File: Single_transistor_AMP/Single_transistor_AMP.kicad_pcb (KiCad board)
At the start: 2 copper layers, 1 part, among them Q1 BC337

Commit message: Pabeigts 7.lekcijas treniņuzdevums (P.Settings, L.Setup, D.Rules)
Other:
- net class Power added: clearance 0.5, trace_width 0.3, via_dia 1, via_drill 0.6
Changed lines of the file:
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@@
-(kicad_pcb (version 20171130) (host pcbnew "(5.1.0)-1")
+(kicad_pcb (version 20171130) (host pcbnew "(5.0.1)-4")
   (general
     (thickness 1.6)
@@
   )
   (page A4)
+  (title_block
+    (title Single_transistor_AMP)
+    (date 2019-05-03)
+    (rev v1.0)
+    (company "Ventspils Augstskola")
+    (comment 1 Autors)
+    (comment 2 "Edgars Irbiņš")
+    (comment 3 "PCB_CAD kurss")
+  )
   (layers
     (0 F.Cu signal)
@@
     (zone_45_only no)
     (trace_min 0.2)
+    (segment_width 0.2)
+    (edge_width 0.05)
     (via_size 0.8)
     (via_drill 0.4)
@@
     (uvia_min_size 0.2)
     (uvia_min_drill 0.1)
-    (edge_width 0.05)
-    (segment_width 0.2)
     (pcb_text_width 0.3)
     (pcb_text_size 1.5 1.5)
@@
     (solder_mask_min_width 0.25)
     (aux_axis_origin 0 0)
-    (visible_elements FFFFFF7F)
+    (visible_elements 7FFFFFFF)
     (pcbplotparams
       (layerselection 0x010fc_ffffffff)
@@
     (add_net "Net-(J2-Pad2)")
   )
+  (net_class Power ""
+    (clearance 0.5)
+    (trace_width 0.3)
+    (via_dia 1)
+    (via_drill 0.6)
+    (uvia_dia 0.3)
+    (uvia_drill 0.1)
+  )
   (module Package_TO_SOT_THT:TO-92_Inline (layer F.Cu)

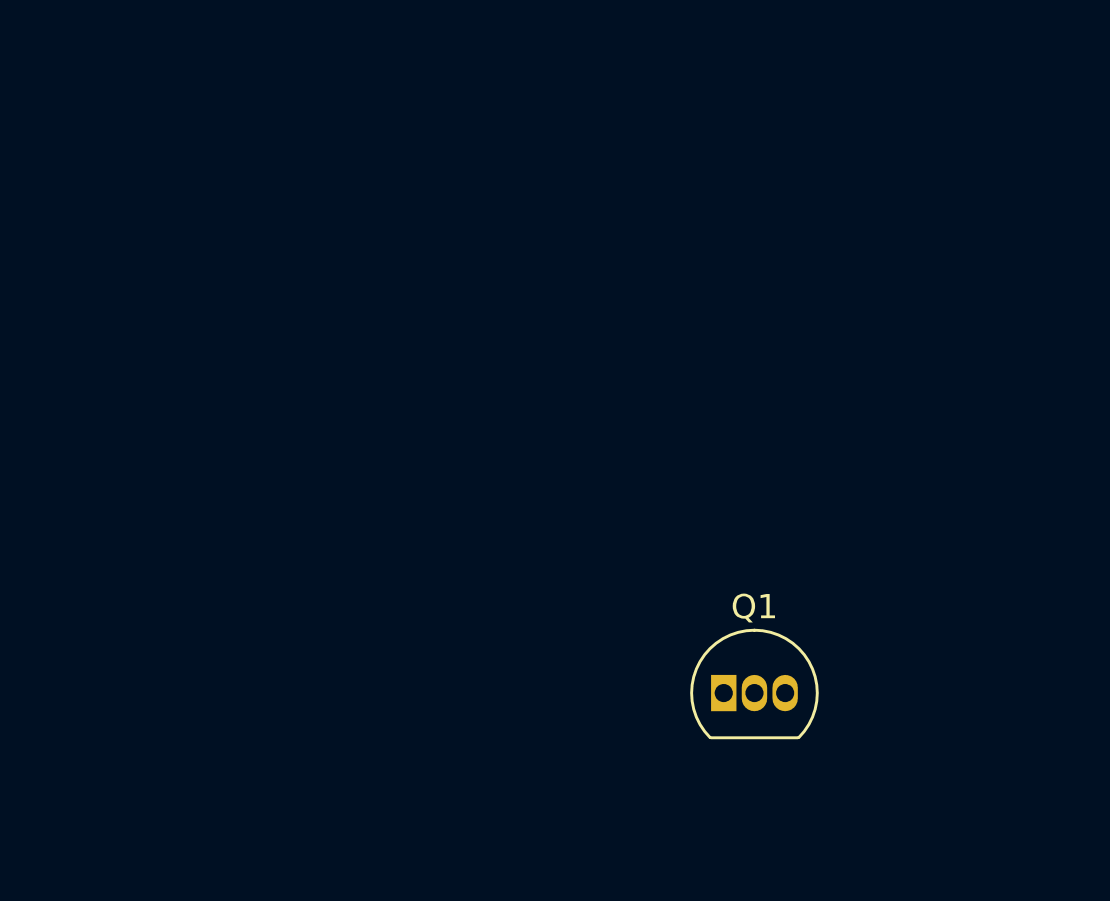
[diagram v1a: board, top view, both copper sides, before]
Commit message: Papildināts Single_transistor_AMP projekts, pēc 8.lekcijas m.d. nosacījumiem (darbs ar Pcbnew)
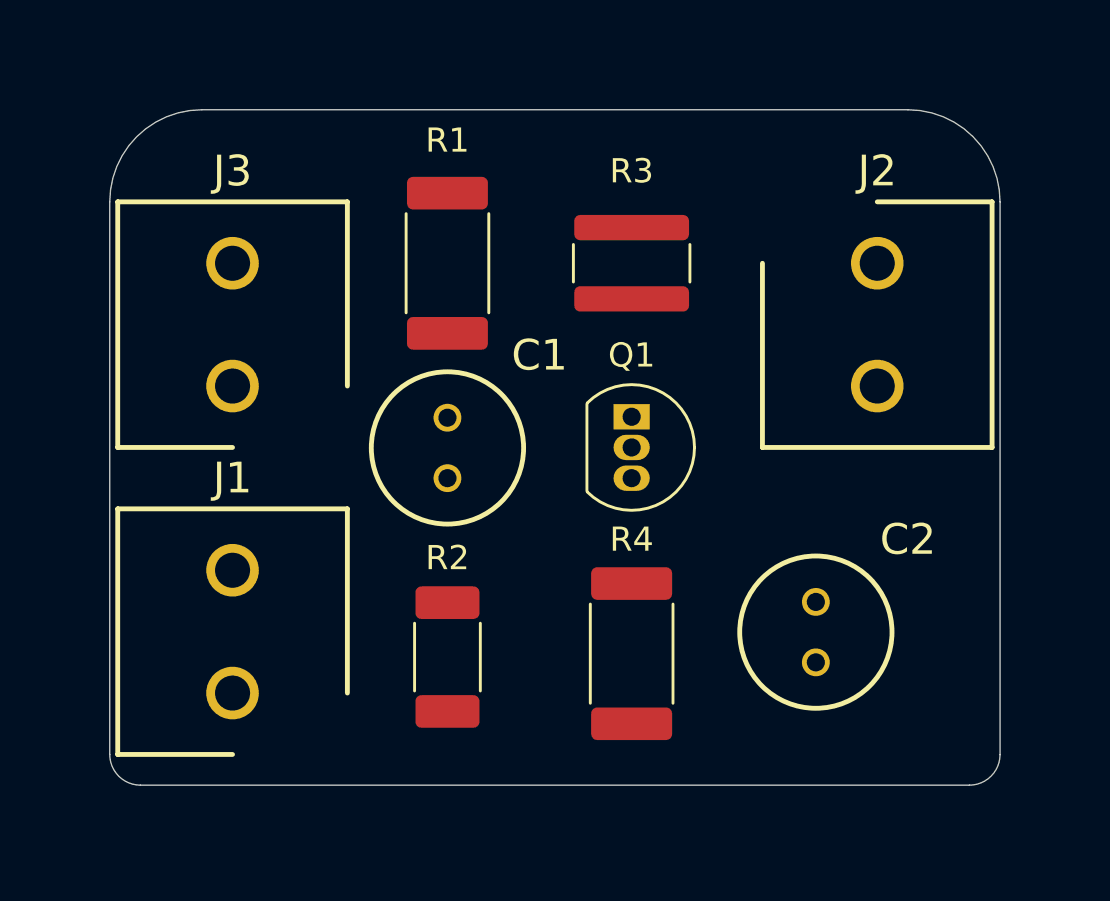
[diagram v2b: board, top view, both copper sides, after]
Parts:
- added C1: 47uF, Single_transistor_AMP:CAPPRD250W55D630H600, F.Cu at (142.2, 101.6)
- added C2: 47uF, Single_transistor_AMP:CAPPRD250W55D630H600, F.Cu at (157.5, 109.2)
- added J1: Signal_IN, Single_transistor_AMP:SHDR2W90P0X508_1X2_1016X950X1500P_Conn, F.Cu at (133.3, 110.5)
- added J2: Signal_OUT, Single_transistor_AMP:SHDR2W90P0X508_1X2_1016X950X1500P_Conn, F.Cu at (160.0, 92.7)
- added J3: +12V_IN, Single_transistor_AMP:SHDR2W90P0X508_1X2_1016X950X1500P_Conn, F.Cu at (133.3, 97.8)
- added R1: 51k, Single_transistor_AMP:R_2512_6332Metric, F.Cu at (142.2, 92.7)
- added R2: 7,1k, Single_transistor_AMP:R_2010_5025Metric, F.Cu at (142.2, 109.0)
- added R3: 1k, Single_transistor_AMP:R_1218_3246Metric, F.Cu at (149.9, 92.7)
- added R4: 100R, Single_transistor_AMP:R_2512_6332Metric, F.Cu at (149.9, 108.9)
- moved Q1 12.0 mm to (149.9, 99.1), turned to 270 degrees
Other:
- board outline added: 36.8 x 27.9 mm

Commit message: Pabeigts 9.lekcijā norādītais mājasdarbs
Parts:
- C1: footprint Single_transistor_AMP:CAPPRD250W55D630H600 -> Single_transistor_AMP:CAPC1608X120N
- moved R3 1.49 mm to (150.4, 91.3)
- moved C1 0.90 mm to (142.8, 100.9)
- moved C2 0.88 mm to (157.9, 108.5)
- moved R2 0.65 mm to (142.8, 109.4)
- moved J2 0.51 mm to (159.5, 92.8)
- moved J1 0.51 mm to (133.9, 110.5)
- moved J3 0.51 mm to (133.9, 97.8)
- moved Q1 0.51 mm to (150.4, 99.1)
- moved R1 0.51 mm to (142.7, 92.7)
- moved R4 0.51 mm to (150.4, 108.9)
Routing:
- net GND: track 0.00 -> 26.4 mm, vias 0 -> 19
- net +12V: track 0.00 -> 20.9 mm
- net Net-(C1-Pad1): track 0.00 -> 20.3 mm
- net Net-(J2-Pad1): track 0.00 -> 14.9 mm
- net Net-(C2-Pad2): track 0.00 -> 11.9 mm
- net Net-(C1-Pad2): track 0.00 -> 11.1 mm
- added copper zone on B.Cu, net GND
- added copper zone on F.Cu, net GND
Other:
- board size 36.8 x 27.9 mm -> 36.8 x 29.2 mm
- board text added: "GND"

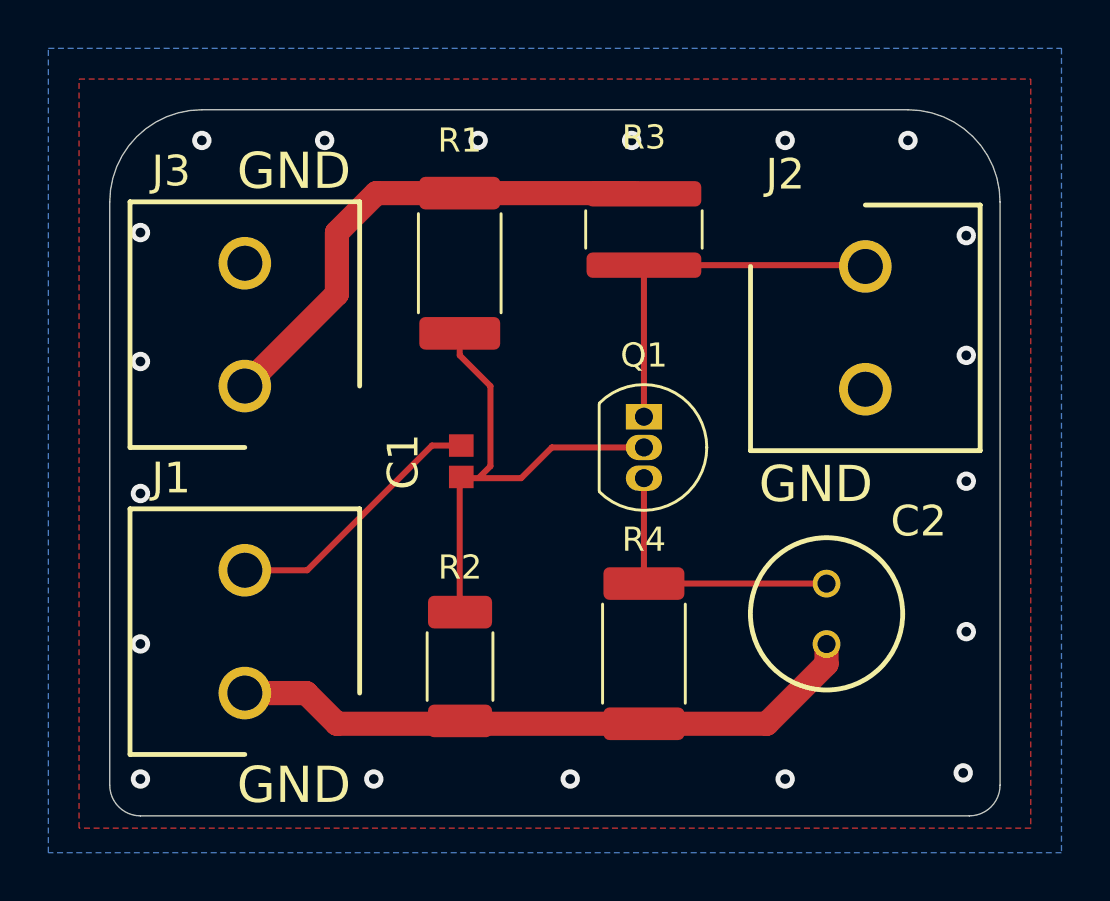
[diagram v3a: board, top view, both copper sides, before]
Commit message: Pabeigts 10.lekcijas m.d. (iegūti Gerber faili)
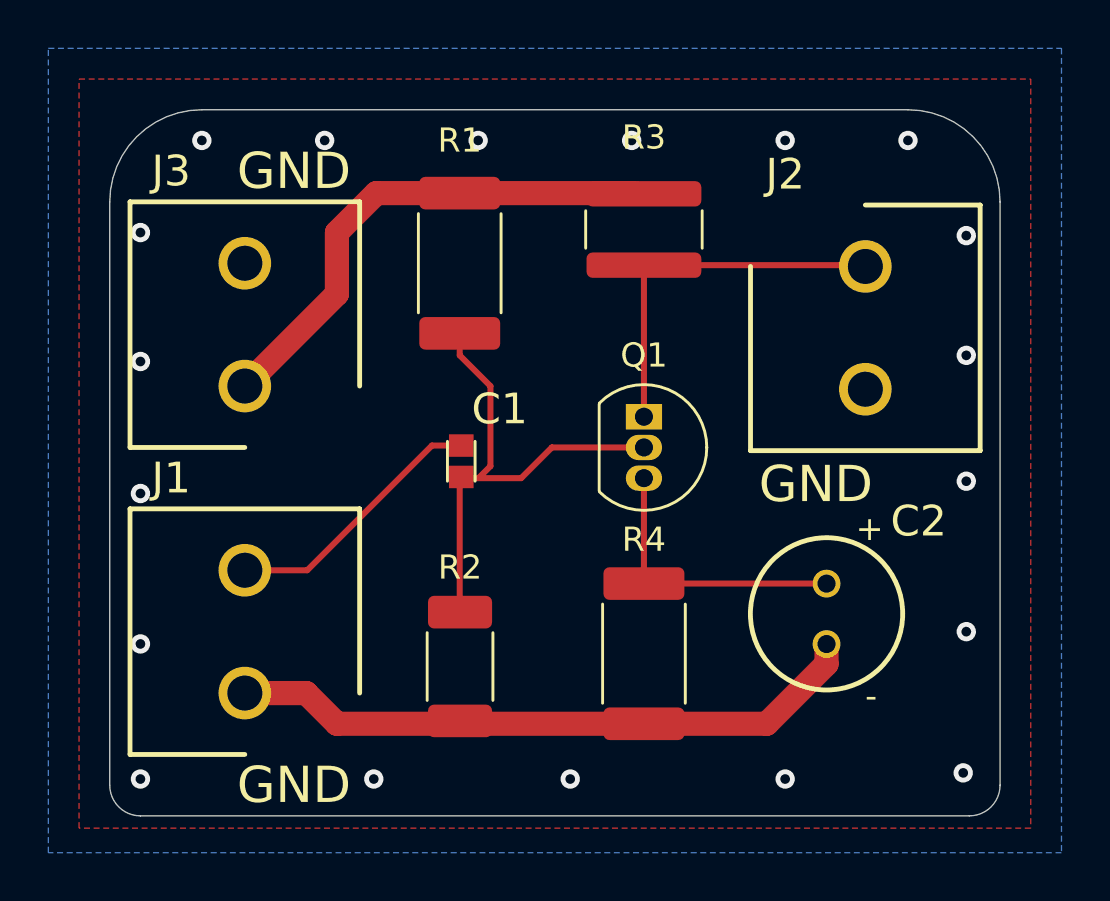
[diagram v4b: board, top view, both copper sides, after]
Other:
- board text added: "+"
- board text added: "-"
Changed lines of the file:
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@@
   (general
     (thickness 1.6)
-    (drawings 15)
+    (drawings 19)
     (tracks 49)
     (zones 0)
@@
   (layers
     (0 F.Cu signal)
-    (31 B.Cu power)
-    (32 B.Adhes user)
-    (33 F.Adhes user)
-    (34 B.Paste user)
-    (35 F.Paste user)
-    (36 B.SilkS user)
+    (31 B.Cu power hide)
+    (32 B.Adhes user hide)
+    (33 F.Adhes user hide)
+    (34 B.Paste user hide)
+    (35 F.Paste user hide)
+    (36 B.SilkS user hide)
     (37 F.SilkS user)
-    (38 B.Mask user)
-    (39 F.Mask user)
+    (38 B.Mask user hide)
+    (39 F.Mask user hide)
     (40 Dwgs.User user hide)
-    (41 Cmts.User user)
-    (42 Eco1.User user)
-    (43 Eco2.User user)
-    (44 Edge.Cuts user)
-    (45 Margin user)
-    (46 B.CrtYd user)
-    (47 F.CrtYd user)
-    (48 B.Fab user)
+    (41 Cmts.User user hide)
+    (42 Eco1.User user hide)
+    (43 Eco2.User user hide)
+    (44 Edge.Cuts user hide)
+    (45 Margin user hide)
+    (46 B.CrtYd user hide)
+    (47 F.CrtYd user hide)
+    (48 B.Fab user hide)
     (49 F.Fab user)
   )
@@
     (visible_elements 7FFFFFFF)
     (pcbplotparams
-      (layerselection 0x010fc_ffffffff)
+      (layerselection 0x010e8_ffffffff)
       (usegerberextensions false)
       (usegerberattributes false)
@@
       (psa4output false)
       (plotreference true)
-      (plotvalue true)
+      (plotvalue false)
       (plotinvisibletext false)
       (padsonsilk false)
@@
       (outputformat 1)
       (mirror false)
-      (drillshape 1)
+      (drillshape 0)
       (scaleselection 1)
       (outputdirectory ""))
@@
       (effects (font (size 1 1) (thickness 0.15)))
     )
-    (fp_text user %R (at 1.27 -2.48 90) (layer F.Fab)
+    (fp_text user %R (at 1.27 -0.1905 90) (layer F.Fab)
       (effects (font (size 1 1) (thickness 0.15)))
     )
@@
       (effects (font (size 1.27 1.27) (thickness 0.254)))
     )
-    (fp_text value 47uF (at 1.524 2.54 90) (layer F.Fab) hide
+    (fp_text value 47uF (at 1.33858 0.12954 90) (layer F.Fab) hide
       (effects (font (size 1.27 1.27) (thickness 0.254)))
     )
@@
     (tags Capacitor)
     (attr smd)
-    (fp_text reference C1 (at -0.02 -2.4 90) (layer F.SilkS)
-      (effects (font (size 1.27 1.27) (thickness 0.254)))
-    )
-    (fp_text value 47uF (at 0.15 2.5 90) (layer F.SilkS) hide
+    (fp_text reference C1 (at 2.159 1.5875 180) (layer F.SilkS)
+      (effects (font (size 1.27 1.27) (thickness 0.254)))
+    )
+    (fp_text value 47uF (at 0.0635 -1.778 90) (layer F.Fab) hide
       (effects (font (size 1.27 1.27) (thickness 0.254)))
     )
@@
       (net 3 "Net-(C1-Pad2)"))
   )
+  (gr_text - (at 159.766 110.617) (layer F.SilkS)
+    (effects (font (size 1 1) (thickness 0.15)))
+  )
+  (gr_text + (at 159.7025 103.6955) (layer F.SilkS)
+    (effects (font (size 1 1) (thickness 0.15)))
+  )
+  (gr_line (start 143.383 100.076) (end 143.383 101.727) (layer F.SilkS) (width 0.12))
+  (gr_line (start 142.24 100.076) (end 142.24 101.727) (layer F.SilkS) (width 0.12))
   (gr_text GND (at 157.48 101.854) (layer F.SilkS)
     (effects (font (size 1.5 1.5) (thickness 0.3)))
